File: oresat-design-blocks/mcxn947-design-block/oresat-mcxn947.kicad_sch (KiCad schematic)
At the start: 1 part, among them IC1 MCXN947VKLT

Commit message: Working on rough draft for MCXN
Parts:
- added C1, C4: 100n, symbol Device:C_Small
- added C2, C3: 4.7p, symbol Device:C_Small
- added J1: Conn_ARM_JTAG_SWD_10, symbol Connector:Conn_ARM_JTAG_SWD_10
- added J2: USB_C_Receptacle_USB2.0_14P, symbol Connector:USB_C_Receptacle_USB2.0_14P
- added R1, R2, R3, R4, R5: 10k, symbol Device:R_Small_US
- added R6, R7: 5.11k, symbol Device:R_Small_US
- added SW1: RESET, Button_Switch_THT:SW_PUSH_6mm, symbol Switch:SW_Push
- added SW2: ISP(BOOT), Button_Switch_THT:SW_PUSH_6mm, symbol Switch:SW_Push
- added Y1: 24M, symbol Device:Crystal_GND23_Small
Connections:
- net at IC1.76 (P0_0): now also J1.2 (SWDIO/TMS), R2.1
- net at IC1.77 (P0_1): now also J1.4 (SWCLK/TCK), R4.2
- net at IC1.78 (P0_2): now also J1.6 (SWO/TDO)
- net at IC1.79 (P0_3): now also J1.8 (NC/TDI), R3.1
- net at IC1.82 (P0_6): now also R5.1, SW2.2
- net at IC1.10 (P1_30): now also C2.1, Y1.4
- net at IC1.11 (P1_31): now also C3.1, Y1.1
- net GND: now reaches IC1.101 (EP)
- net GND: now also C1.2, C2.2, C3.2, C4.2, J1.3 (GND), J1.5 (GND), J1.9 (GNDDetect), J2.A1 (GND), J2.A12 (GND), J2.B1 (GND), J2.B12 (GND), R4.1, R6.1, R7.1, SW1.2, SW2.1, Y1.2, Y1.3
- net RESET: now reaches IC1.9 (RESET_B)
- net RESET: now also C1.1, J1.10 (~{RESET}), R1.1, SW1.1
- new net: J2.B5 (CC2), R7.2
- new net: J2.A5 (CC1), R6.2
- new net: C4.1, J2.S1 (SHIELD)
- new net: J2.A4 (VBUS), J2.A9 (VBUS), J2.B4 (VBUS), J2.B9 (VBUS)
- new net +3.3V: J1.1 (VTref), R1.2, R2.2, R3.2, R5.2
- new net USB_D+: J2.A6 (D+), J2.B6 (D+)
- new net USB_D-: J2.A7 (D-), J2.B7 (D-)
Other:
- company: (none) -> Portland State Aerospace Society
- title: (none) -> MCNX947KVLT Breakout
- moved on the sheet: IC1B, IC1C

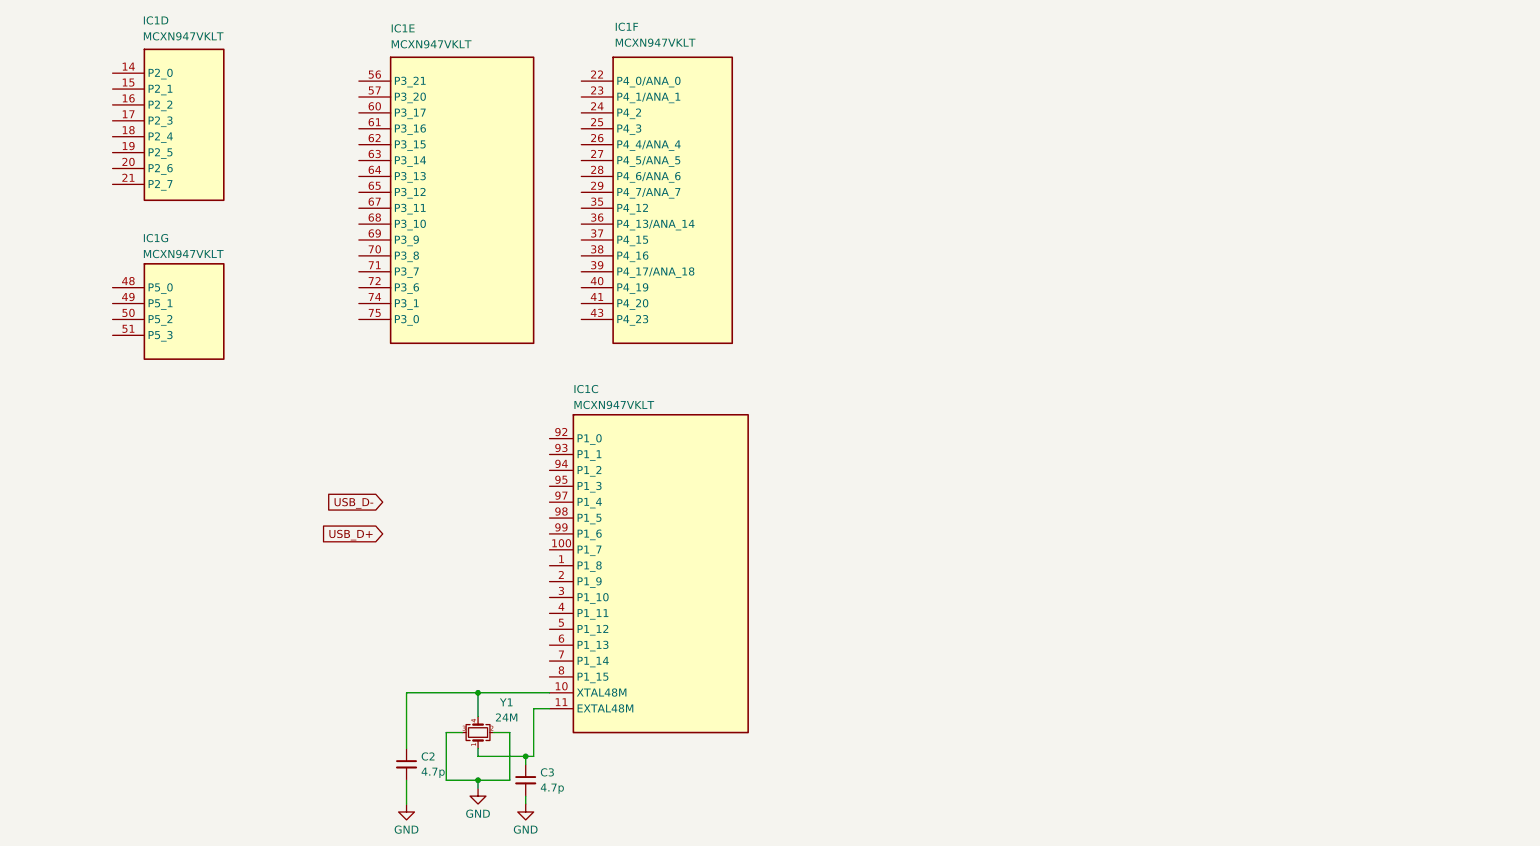
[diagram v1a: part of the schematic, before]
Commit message: Removed lock file, updated .gitignore file
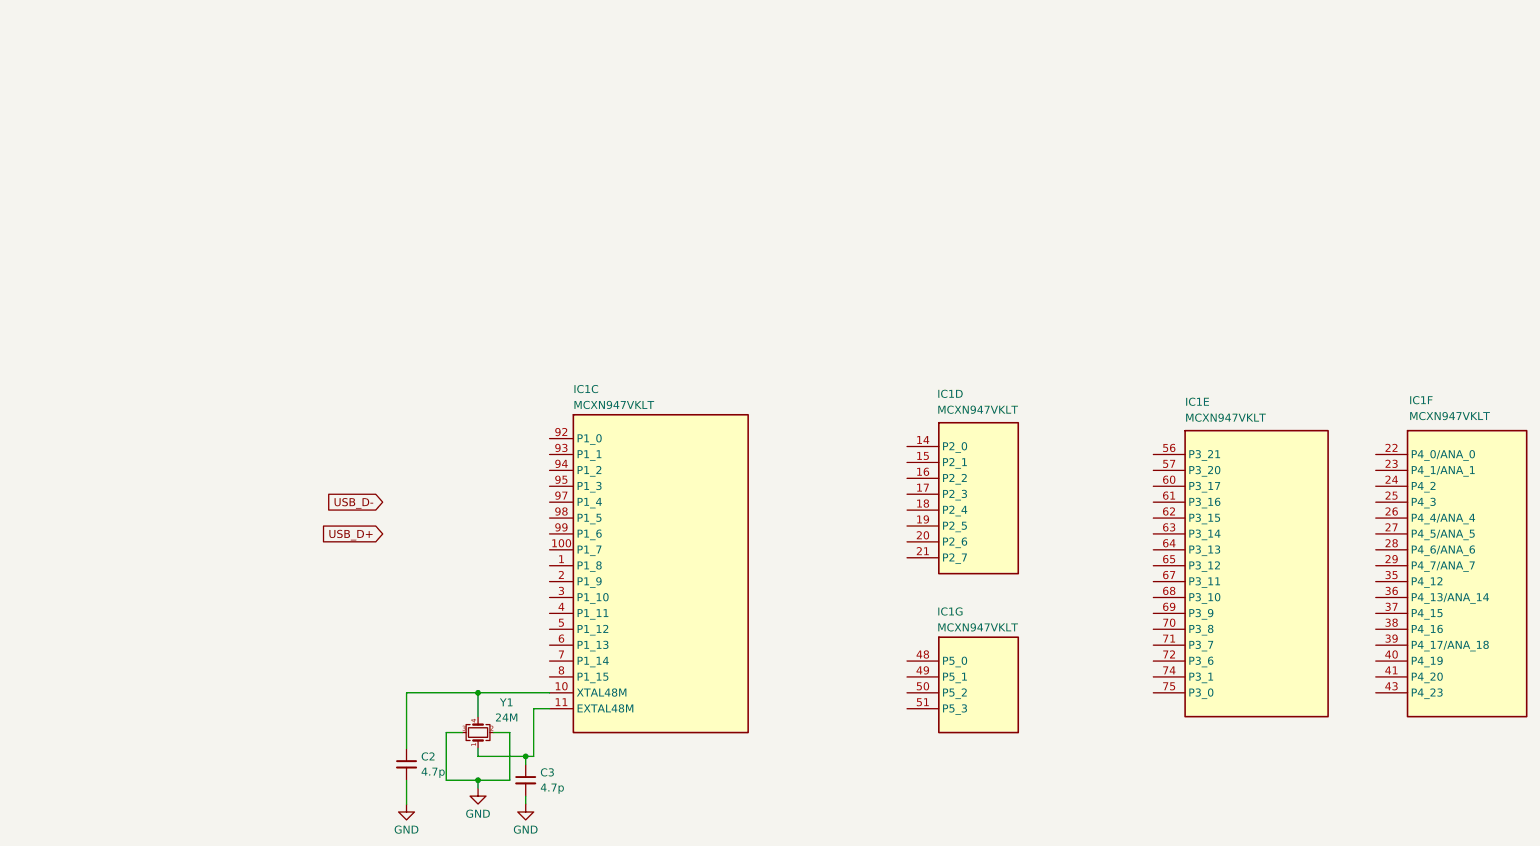
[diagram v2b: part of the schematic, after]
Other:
- moved on the sheet: IC1D, IC1E, IC1F, IC1G
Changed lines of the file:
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@@
 		(lib_name "MCXN947VKLT_3")
 		(lib_id "oresat-ics:MCXN947VKLT")
-		(at 181.61 25.4 0)
+		(at 308.61 85.09 0)
 		(unit 4)
 		(exclude_from_sim no)
@@
 		(dnp no)
 		(property "Reference" "IC1"
-			(at 181.356 20.828 0)
+			(at 308.356 80.518 0)
 			(effects
 				(font
@@
 		)
 		(property "Value" "MCXN947VKLT"
-			(at 181.356 23.368 0)
+			(at 308.356 83.058 0)
 			(effects
 				(font
@@
 		)
 		(property "Footprint" "oresat-ics:MCXN947KVLT-QFP50P1600X1600X160-101N"
-			(at 182.88 -3.81 0)
+			(at 309.88 55.88 0)
 			(effects
 				(font
@@
 		)
 		(property "Datasheet" "https://www.nxp.com/docs/en/data-sheet/MCXNx4xDS.pdf"
-			(at 182.626 2.616 0)
+			(at 309.626 62.306 0)
 			(effects
 				(font
@@
 		)
 		(property "Description" "ARM Microcontrollers - MCU MCXN10, 100HLQFP (also MCXN947VNLT)"
-			(at 206.502 0 0)
+			(at 333.502 59.69 0)
 			(effects
 				(font
@@
 		)
 		(property "Height" "1.6"
-			(at 256.54 410.16 0)
+			(at 383.54 469.85 0)
 			(effects
 				(font
@@
 		)
 		(property "Manufacturer_Name" "NXP"
-			(at 256.54 510.16 0)
+			(at 383.54 569.85 0)
 			(effects
 				(font
@@
 		)
 		(property "Manufacturer_Part_Number" "MCXN947VNLT"
-			(at 256.54 610.16 0)
+			(at 383.54 669.85 0)
 			(effects
 				(font
@@
 		)
 		(property "Mouser Part Number" "771-MCXN947VNLT"
-			(at 256.54 710.16 0)
+			(at 383.54 769.85 0)
 			(effects
 				(font
@@
 		)
 		(property "Mouser Price/Stock" "https://www.mouser.co.uk/ProductDetail/NXP-Semiconductors/MCXN947VNLT?qs=Z%252BL2brAPG1JdBwTv%2FdATDA%3D%3D"
-			(at 256.54 810.16 0)
+			(at 383.54 869.85 0)
 			(effects
 				(font
@@
 		)
 		(property "Arrow Part Number" "MCXN947VNLT"
-			(at 256.54 910.16 0)
+			(at 383.54 969.85 0)
 			(effects
 				(font
@@
 		)
 		(property "Arrow Price/Stock" "https://www.arrow.com/en/products/mcxn947vnlt/nxp-semiconductors?utm_currency=USD&region=nac"
-			(at 256.54 1010.16 0)
+			(at 383.54 1069.85 0)
 			(effects
 				(font
@@
 		)
 		(property "MFR" "NXP"
-			(at 256.54 510.16 0)
+			(at 383.54 569.85 0)
 			(effects
 				(font
@@
 		)
 		(property "MPN" "MCXN947VKLT"
-			(at 256.54 610.16 0)
+			(at 383.54 669.85 0)
 			(effects
 				(font
@@
 		(lib_name "MCXN947VKLT_4")
 		(lib_id "oresat-ics:MCXN947VKLT")
-		(at 181.61 59.69 0)
+		(at 308.61 119.38 0)
 		(unit 7)
 		(exclude_from_sim no)
@@
 		(dnp no)
 		(property "Reference" "IC1"
-			(at 181.356 55.626 0)
+			(at 308.356 115.316 0)
 			(effects
 				(font
@@
 		)
 		(property "Value" "MCXN947VKLT"
-			(at 181.356 58.166 0)
+			(at 308.356 117.856 0)
 			(effects
 				(font
@@
 		)
 		(property "Footprint" "oresat-ics:MCXN947KVLT-QFP50P1600X1600X160-101N"
-			(at 182.88 30.48 0)
+			(at 309.88 90.17 0)
 			(effects
 				(font
@@
 		)
 		(property "Datasheet" "https://www.nxp.com/docs/en/data-sheet/MCXNx4xDS.pdf"
-			(at 182.626 36.906 0)
+			(at 309.626 96.596 0)
 			(effects
 				(font
@@
 		)
 		(property "Description" "ARM Microcontrollers - MCU MCXN10, 100HLQFP (also MCXN947VNLT)"
-			(at 206.502 34.29 0)
+			(at 333.502 93.98 0)
 			(effects
 				(font
@@
 		)
 		(property "Height" "1.6"
-			(at 256.54 444.45 0)
+			(at 383.54 504.14 0)
 			(effects
 				(font
@@
 		)
 		(property "Manufacturer_Name" "NXP"
-			(at 256.54 544.45 0)
+			(at 383.54 604.14 0)
 			(effects
 				(font
@@
 		)
 		(property "Manufacturer_Part_Number" "MCXN947VNLT"
-			(at 256.54 644.45 0)
+			(at 383.54 704.14 0)
 			(effects
 				(font
@@
 		)
 		(property "Mouser Part Number" "771-MCXN947VNLT"
-			(at 256.54 744.45 0)
+			(at 383.54 804.14 0)
 			(effects
 				(font
@@
 		)
 		(property "Mouser Price/Stock" "https://www.mouser.co.uk/ProductDetail/NXP-Semiconductors/MCXN947VNLT?qs=Z%252BL2brAPG1JdBwTv%2FdATDA%3D%3D"
-			(at 256.54 844.45 0)
+			(at 383.54 904.14 0)
 			(effects
 				(font
@@
 		)
 		(property "Arrow Part Number" "MCXN947VNLT"
-			(at 256.54 944.45 0)
+			(at 383.54 1004.14 0)
 			(effects
 				(font
@@
 		)
 		(property "Arrow Price/Stock" "https://www.arrow.com/en/products/mcxn947vnlt/nxp-semiconductors?utm_currency=USD&region=nac"
-			(at 256.54 1044.45 0)
+			(at 383.54 1104.14 0)
 			(effects
 				(font
@@
 		)
 		(property "MFR" "NXP"
-			(at 256.54 544.45 0)
+			(at 383.54 604.14 0)
 			(effects
 				(font
@@
 		)
 		(property "MPN" "MCXN947VKLT"
-			(at 256.54 644.45 0)
+			(at 383.54 704.14 0)
 			(effects
 				(font
@@
 	)
 	(symbol
-		(lib_name "MCXN947VKLT_1")
+		(lib_name "MCXN947VKLT_3")
 		(lib_id "oresat-ics:MCXN947VKLT")
-		(at 220.98 26.67 0)
+		(at 347.98 86.36 0)
 		(unit 5)
 		(exclude_from_sim no)
@@
 		(dnp no)
 		(property "Reference" "IC1"
-			(at 220.98 22.098 0)
+			(at 347.98 81.788 0)
 			(effects
 				(font
@@
 		)
 		(property "Value" "MCXN947VKLT"
-			(at 220.98 24.638 0)
+			(at 347.98 84.328 0)
 			(effects
 				(font
@@
 		)
 		(property "Footprint" "oresat-ics:MCXN947KVLT-QFP50P1600X1600X160-101N"
-			(at 222.25 -2.54 0)
+			(at 349.25 57.15 0)
 			(effects
 				(font
@@
 		)
 		(property "Datasheet" "https://www.nxp.com/docs/en/data-sheet/MCXNx4xDS.pdf"
-			(at 221.996 3.886 0)
+			(at 348.996 63.576 0)
 			(effects
 				(font
@@
 		)
 		(property "Description" "ARM Microcontrollers - MCU MCXN10, 100HLQFP (also MCXN947VNLT)"
-			(at 245.872 1.27 0)
+			(at 372.872 60.96 0)
 			(effects
 				(font
@@
 		)
 		(property "Height" "1.6"
-			(at 295.91 411.43 0)
+			(at 422.91 471.12 0)
 			(effects
 				(font
@@
 		)
 		(property "Manufacturer_Name" "NXP"
-			(at 295.91 511.43 0)
+			(at 422.91 571.12 0)
 			(effects
 				(font
@@
 		)
 		(property "Manufacturer_Part_Number" "MCXN947VNLT"
-			(at 295.91 611.43 0)
+			(at 422.91 671.12 0)
 			(effects
 				(font
@@
 		)
 		(property "Mouser Part Number" "771-MCXN947VNLT"
-			(at 295.91 711.43 0)
+			(at 422.91 771.12 0)
 			(effects
 				(font
@@
 		)
 		(property "Mouser Price/Stock" "https://www.mouser.co.uk/ProductDetail/NXP-Semiconductors/MCXN947VNLT?qs=Z%252BL2brAPG1JdBwTv%2FdATDA%3D%3D"
-			(at 295.91 811.43 0)
+			(at 422.91 871.12 0)
 			(effects
 				(font
@@
 		)
 		(property "Arrow Part Number" "MCXN947VNLT"
-			(at 295.91 911.43 0)
+			(at 422.91 971.12 0)
 			(effects
 				(font
@@
 		)
 		(property "Arrow Price/Stock" "https://www.arrow.com/en/products/mcxn947vnlt/nxp-semiconductors?utm_currency=USD&region=nac"
-			(at 295.91 1011.43 0)
+			(at 422.91 1071.12 0)
 			(effects
 				(font
@@
 		)
 		(property "MFR" "NXP"
-			(at 295.91 511.43 0)
+			(at 422.91 571.12 0)
 			(effects
 				(font
@@
 		)
 		(property "MPN" "MCXN947VKLT"
-			(at 295.91 611.43 0)
+			(at 422.91 671.12 0)
 			(effects
 				(font
@@
 		(lib_name "MCXN947VKLT_6")
 		(lib_id "oresat-ics:MCXN947VKLT")
-		(at 256.54 26.67 0)
+		(at 383.54 86.36 0)
 		(unit 6)
 		(exclude_from_sim no)
@@
 		(dnp no)
 		(property "Reference" "IC1"
-			(at 256.794 21.844 0)
+			(at 383.794 81.534 0)
 			(effects
 				(font
@@
 		)
 		(property "Value" "MCXN947VKLT"
-			(at 256.794 24.384 0)
+			(at 383.794 84.074 0)
 			(effects
 				(font
@@
 		)
 		(property "Footprint" "oresat-ics:MCXN947KVLT-QFP50P1600X1600X160-101N"
-			(at 257.81 -2.54 0)
+			(at 384.81 57.15 0)
 			(effects
 				(font
@@
 		)
 		(property "Datasheet" "https://www.nxp.com/docs/en/data-sheet/MCXNx4xDS.pdf"
-			(at 257.556 3.886 0)
+			(at 384.556 63.576 0)
 			(effects
 				(font
@@
 		)
 		(property "Description" "ARM Microcontrollers - MCU MCXN10, 100HLQFP (also MCXN947VNLT)"
-			(at 281.432 1.27 0)
+			(at 408.432 60.96 0)
 			(effects
 				(font
@@
 		)
 		(property "Height" "1.6"
-			(at 331.47 411.43 0)
+			(at 458.47 471.12 0)
 			(effects
 				(font
@@
 		)
 		(property "Manufacturer_Name" "NXP"
-			(at 331.47 511.43 0)
+			(at 458.47 571.12 0)
 			(effects
 				(font
@@
 		)
 		(property "Manufacturer_Part_Number" "MCXN947VNLT"
-			(at 331.47 611.43 0)
+			(at 458.47 671.12 0)
 			(effects
 				(font
@@
 		)
 		(property "Mouser Part Number" "771-MCXN947VNLT"
-			(at 331.47 711.43 0)
+			(at 458.47 771.12 0)
 			(effects
 				(font
@@
 		)
 		(property "Mouser Price/Stock" "https://www.mouser.co.uk/ProductDetail/NXP-Semiconductors/MCXN947VNLT?qs=Z%252BL2brAPG1JdBwTv%2FdATDA%3D%3D"
-			(at 331.47 811.43 0)
+			(at 458.47 871.12 0)
 			(effects
 				(font
@@
 		)
 		(property "Arrow Part Number" "MCXN947VNLT"
-			(at 331.47 911.43 0)
+			(at 458.47 971.12 0)
 			(effects
 				(font
@@
 		)
 		(property "Arrow Price/Stock" "https://www.arrow.com/en/products/mcxn947vnlt/nxp-semiconductors?utm_currency=USD&region=nac"
-			(at 331.47 1011.43 0)
+			(at 458.47 1071.12 0)
 			(effects
 				(font
@@
 		)
 		(property "MFR" "NXP"
-			(at 331.47 511.43 0)
+			(at 458.47 571.12 0)
 			(effects
 				(font
@@
 		)
 		(property "MPN" "MCXN947VKLT"
-			(at 331.47 611.43 0)
-			(effects
-				(font
+			(at 458.47 671.12 0)
+			(effects
+				(font

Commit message: Rough draft of MCXN design block / breakout board
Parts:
- added C10, C12: 4.7u, symbol Device:C_Small
- added C11: 1u, symbol Device:C_Small
- added C5: 100n, symbol Device:C_Small
- added C6, C7: 4.7p, symbol Device:C_Small
- added C8: 2.2u, symbol Device:C_Small
- added C9: 6.8u, symbol Device:C_Small
- added D1: BAT54CW, Package_TO_SOT_SMD:SOT-323_SC-70, symbol Diode:BAT54CW
- added FB1: 120 ohm ?, symbol Device:FerriteBead_Small
- added J3: FTDI-UART-6PIN, Connector_PinHeader_2.54mm:PinHeader_1x06_P2.54mm_Vertical, symbol oresat-connectors:FTDI-UART-6PIN
- added J4: CAN, symbol Connector_Generic:Conn_01x04
- added J5: TERM, symbol Connector_Generic:Conn_01x02
- added J6: BKUP-BATT, symbol Connector_Generic:Conn_01x02
- added L1: 1.5u, symbol Device:L_Small
- added R8, R9: 60.4, symbol Device:R_Small_US
- added TP1, TP10, TP2, TP3, TP4, TP5, TP6, TP7, TP8, TP9: Test-Point, oresat-misc:TestPoint-0.75mm-th, symbol oresat-misc:Test-Point-0.75mm-th
- added U1: TCAN330, symbol Interface_CAN_LIN:TCAN330
- added Y2: 830009678, symbol Device:Crystal_Small
- J1: value Conn_ARM_JTAG_SWD_10 -> 10pin ARM SWD
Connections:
- net +3.3V: now also IC1.34 (VDD_P4), IC1.44 (VDD_USB), IC1.54 (VDD_DCDC/VDD_LDO_SYS), IC1.59 (VDD_P3_1), IC1.66 (VDD_P3_2), IC1.73 (VDD_P3_3), IC1.83 (VDD_1), IC1.96 (VDD_2), C10.1, C5.1, D1.2, FB1.1, J4.1 (Pin_1), U1.3 (VCC)
- net GND: now also IC1.32 (VREFL), IC1.33 (VSS_P4), IC1.52 (VSS_DCDC), C10.2, C11.2, C12.2, C5.2, C6.1, C7.1, C8.2, C9.2, J3.1 (GND), J4.4 (Pin_4), J6.2 (Pin_2), U1.2 (GND)
- net RESET: now also TP7.1
- net USB_D+: now also IC1.46 (USB0_DP)
- net USB_D-: now also IC1.45 (USB0_DM)
- net SWDIO: now reaches IC1.76 (P0_0), J1.2 (SWDIO/TMS), R2.1
- net SWCLK: now reaches IC1.77 (P0_1), J1.4 (SWCLK/TCK), R4.2
- net SWO: now reaches IC1.78 (P0_2), J1.6 (SWO/TDO)
- net SWI: now reaches IC1.79 (P0_3), J1.8 (NC/TDI), R3.1
- net BOOT: now reaches IC1.82 (P0_6), R5.1, SW2.2
- net BOOT: now also TP10.1
- net FC4_UART_RXD: now reaches IC1.1 (P1_8)
- net FC4_UART_RXD: now also J3.4 (TXD), TP8.1
- net FC4_UART_TXD: now reaches IC1.2 (P1_9)
- net FC4_UART_TXD: now also J3.5 (RXD), TP9.1
- net CAN_TXD: now reaches IC1.3 (P1_10)
- net CAN_TXD: now also U1.1 (TXD)
- net CAN_RXD: now reaches IC1.4 (P1_11)
- net CAN_RXD: now also U1.4 (RXD)
- net at IC1.48 (P5_0): now also C6.2, Y2.2
- net at IC1.49 (P5_1): now also C7.2, Y2.1
- net VBUS: now reaches IC1.35 (P4_12)
- net VBUS: now also J2.A4 (VBUS), J2.A9 (VBUS), J2.B4 (VBUS), J2.B9 (VBUS)
- net at IC1.12 (VDD_CORE_1): now also IC1.13 (VDD_LDO_CORE/VDD/VDD_P2), IC1.58 (VDD_CORE_2), C12.1, C9.1, L1.1, TP4.1
- net at IC1.30 (VDD_ANA): now also IC1.31 (VREFH), C11.1, FB1.2, TP5.1
- net at IC1.47 (VDD_BAT): now also D1.3, TP6.1
- net at IC1.53 (DCDC_LX): now also L1.2
- net at IC1.55 (VDD_SYS): now also C8.1
- new net: TP3.1, U1.8 (S)
- new net: J5.1 (Pin_1), R8.1
- new net: J5.2 (Pin_2), R9.2
- new net: TP2.1, U1.5 (SHDN)
- new net: D1.1, J6.1 (Pin_1)
- new net: J3.3 (VCC), TP1.1
- new net CANH: J4.2 (Pin_2), R9.1, U1.7 (CANH)
- new net CANL: J4.3 (Pin_3), R8.2, U1.6 (CANL)
- no-connect marks 0 -> 2
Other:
- note added: "CAN (MCXN ISP)"
- note added: "FTDI 6pin cable interface UART (MCXN ISP)"
- note added: "ISP CAN"
- note added: "ISP I2C"
- note added: "ISP SPI"
- note added: "ISP UART"
- note added: "MAYBE 5V?"
- note added: "P0/P1"
- note added: "See also USB0_VBUS_DET"
- note added: "USB0_VUS_DET"
- moved on the sheet: C1, C2, C3, C4, IC1A, IC1B, IC1C, IC1D, IC1E, IC1F, IC1G, J1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
